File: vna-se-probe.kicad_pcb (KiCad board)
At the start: 2 copper layers, 18.8 x 11.6 mm, 5 parts, among them J2 Harwin_1x1_H2.4mm_Pad1.7mm_P7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, J3 Harwin_1x1_H2.4mm_Pad1.7mm_P7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, J4 Conn_SMA_RF2-143-T-17-50-G

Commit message: [#75263] Update project
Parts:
- removed the G*** at (140.4, 88.8)
- added G***: LOGO, antmicro-footprints:antmicro-logo_scaled_12mm_silk, F.Cu at (140.6, 88.9)
- J3: moved to F.Cu
- moved J2 0.20 mm to (133.5, 85.2)
- moved J3 0.20 mm to (133.5, 87.8), turned to 0 degrees
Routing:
- net Net-(J2-Pad1): vias 1 -> 0
- net GND: vias 27 -> 34
- added copper zone on In1.Cu, net GND
- added copper zone on In2.Cu, net GND
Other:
- outline, holes or cut-outs redrawn
- copper layers 2 -> 4
- board text added: "04/2025 Rev. 1.0.0"
- board text added: "SHA: ########"
- board text added: "VNA SE probe"
- board text removed: "04/2025"
- board text removed: "Rev. 1.0.0"
- board text removed: "VNA SE"
- board text removed: "probe"

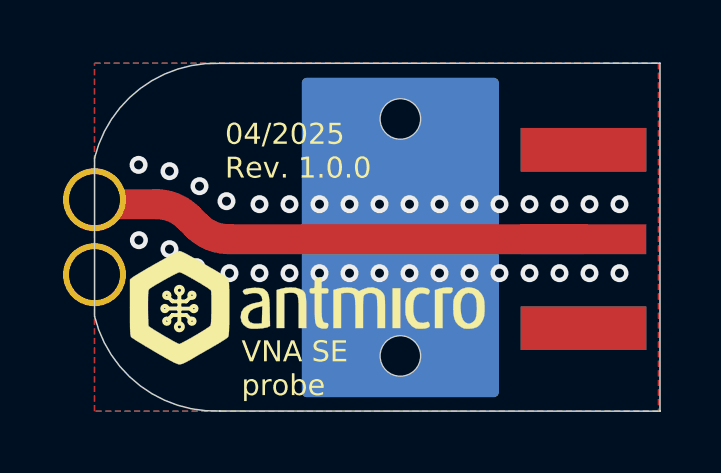
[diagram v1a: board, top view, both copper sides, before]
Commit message: [#75263] Add test needles support
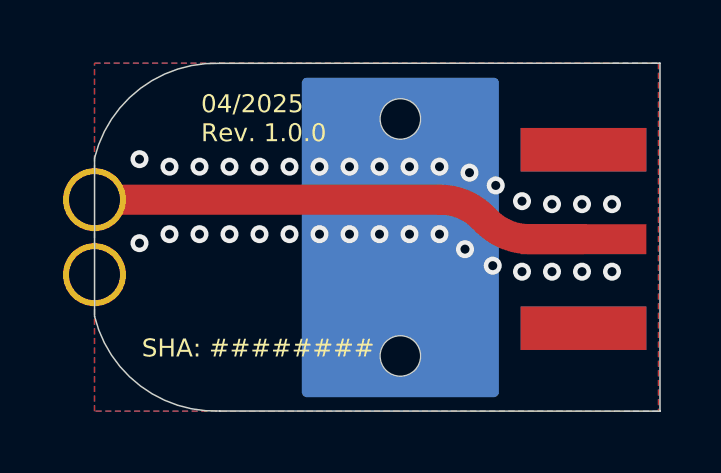
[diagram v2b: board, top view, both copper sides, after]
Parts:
- G***: moved to B.Cu
- ORIN_AGX: renamed from J4; value Conn_SMA_RF2-143-T-17-50-G -> ORIN_AGX
- moved G*** 3.66 mm to (137.7, 86.6), turned to 90 degrees

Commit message: [#75263] Adjust via, clean DRC and ERC
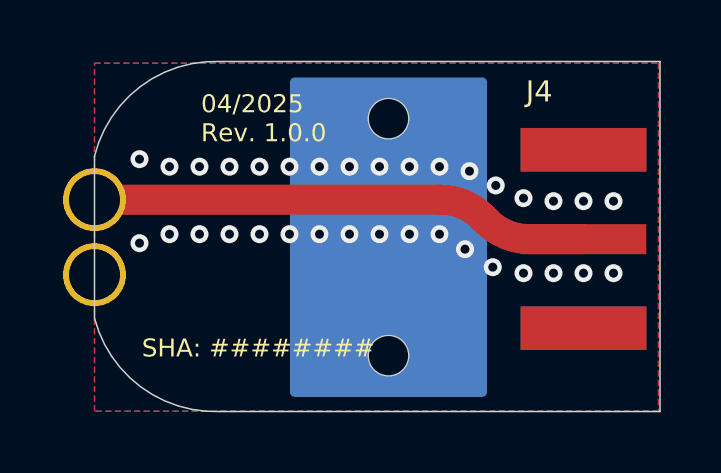
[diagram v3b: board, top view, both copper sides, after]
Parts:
- removed ORIN_AGX: ORIN_AGX, antmicro-footprints:RF_SMA_BoardEdge_RF2-143-T-17-50-G
- added J4: Conn_SMA_RF2-143-T-17-50-G, antmicro-footprints:RF_SMA_BoardEdge_RF2-143-T-17-50-G, F.Cu at (154.8, 86.6)
- moved H1 0.40 mm to (143.3, 86.5)
- moved G*** 0.22 mm to (137.5, 86.6)
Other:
- board size 18.8 x 11.6 mm -> 18.9 x 11.7 mm

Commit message: [#75263] Update silkscreen, align pogopin, clean DRC
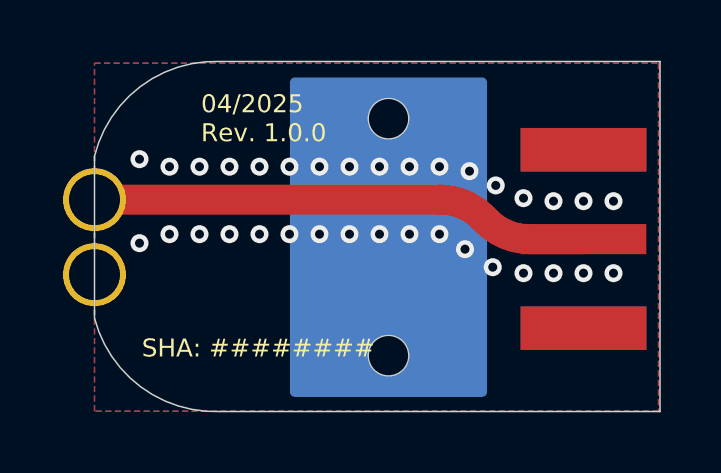
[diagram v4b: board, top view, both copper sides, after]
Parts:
- J2: moved to F.Cu
- turned J2 to 0 degrees

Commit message: [#75263] Update annular ring and via placement
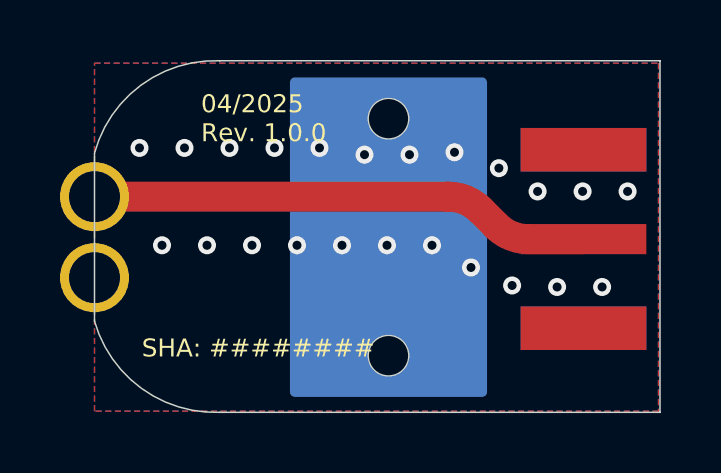
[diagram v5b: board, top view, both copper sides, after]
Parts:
- moved J2 0.10 mm to (133.5, 85.2)
- moved J3 0.10 mm to (133.5, 87.8)
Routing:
- net GND: vias 34 -> 23
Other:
- board size 18.9 x 11.7 mm -> 18.8 x 11.7 mm

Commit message: [#80183] Update pogo pin lib link
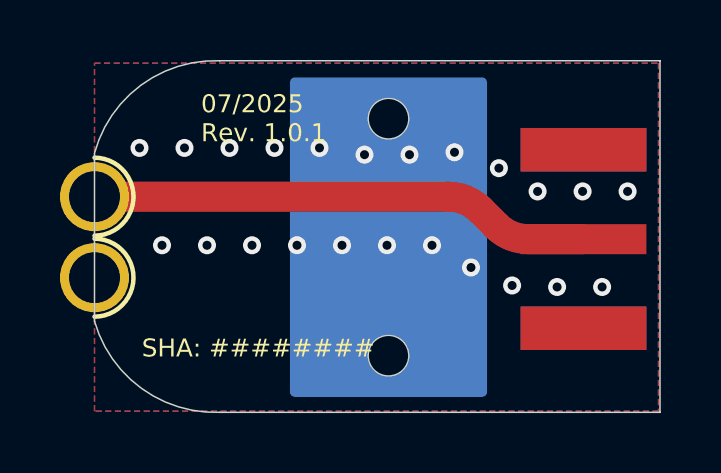
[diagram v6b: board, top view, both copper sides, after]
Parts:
- J2, J3: value Harwin_1x1_H2.4mm_Pad1.7mm_P70-5000045R -> Harwin_1x1_H2.4mm_Pad1.7mm_P70-5000045R_Edge; footprint antmicro-footprints:Harwin_1x1_H2.4mm_Pad1.7mm_P70-5000045R -> antmicro-footprints:Harwin_1x1_H2.4mm_Pad1.7mm_P70-5000045R_Edge
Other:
- outline, holes or cut-outs redrawn
- board text added: "07/2025 Rev. 1.0.1"
- board text removed: "04/2025 Rev. 1.0.0"

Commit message: [#80183] Update library links
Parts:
- J2, J3: value Harwin_1x1_H2.4mm_Pad1.7mm_P70-5000045R_Edge -> Harwin_1x1_H2.4mm_Pad1.7mm_P70-5000045R_CUSTOM_EdgeMount; footprint antmicro-footprints:Harwin_1x1_H2.4mm_Pad1.7mm_P70-5000045R_Edge -> antmicro-footprints:Harwin_1x1_H2.4mm_Pad1.7mm_P70-5000045R_CUSTOM_EdgeMount
